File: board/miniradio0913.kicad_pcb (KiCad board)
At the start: 2 copper layers, 33 x 27.9 mm, 28 parts, among them J1 AudioJack3, J2 Conn_01x03_Socket, J3 USB_B_Micro, Q2 Q_PMOS_GSD, SW1 SW_Push, SW2 SW_Push, SW3 SW_Push, U1 CH32V003JxMx, U2 KT0913, U3 AQM0802, Y2 Crystal_GND2

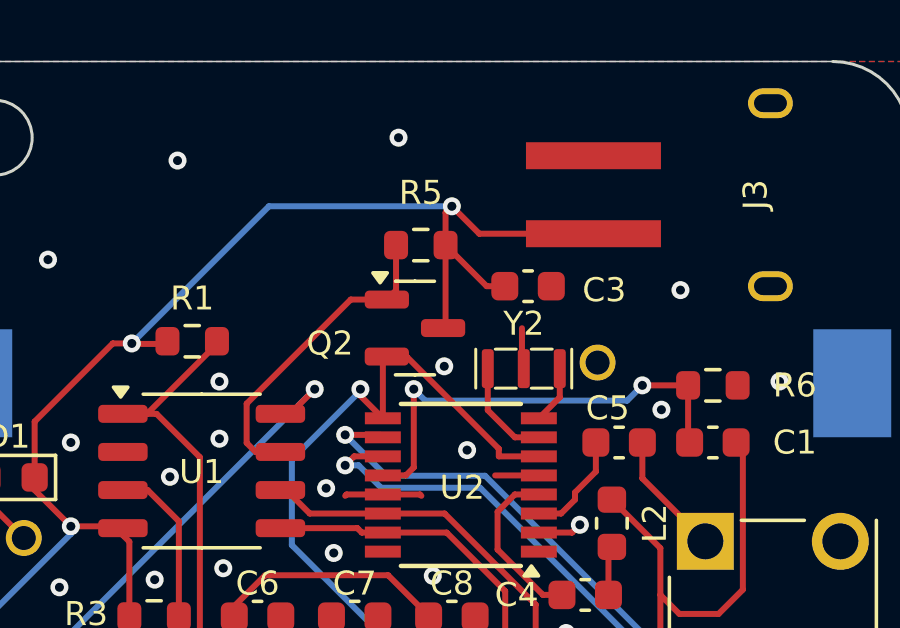
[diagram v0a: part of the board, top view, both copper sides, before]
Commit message: fix(board): crystal
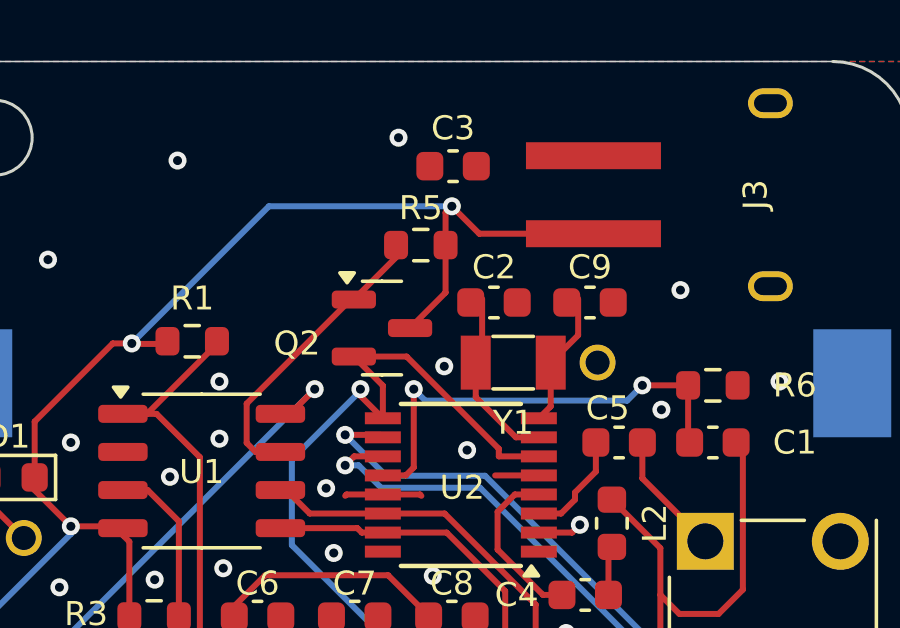
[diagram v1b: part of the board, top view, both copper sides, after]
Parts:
- removed Y2: Crystal_GND2, Library:SMD_Crystal_Murata
- added C2: 15p, Capacitor_SMD:C_0603_1608Metric, F.Cu at (57.3, 24.5)
- added C9: 15p, Capacitor_SMD:C_0603_1608Metric, F.Cu at (60.5, 24.5)
- added Y1: 32.768kHz, Crystal:Crystal_SMD_3215-2Pin_3.2x1.5mm, F.Cu at (57.9, 26.5)
- moved C3 4.72 mm to (55.9, 20.0)
- moved Q2 1.10 mm to (53.5, 25.4)
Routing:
- net Net-(U2-XO): track 1.94 -> 4.53 mm
- net Net-(U2-XI/RCLK): track 3.46 -> 6.03 mm
- net VDD: track 45.4 -> 43.3 mm
- net Net-(Q2-S): track 38.6 -> 40.1 mm
- net GND: track 28.8 -> 27.4 mm
- net Net-(Q2-G): track 10.6 -> 9.97 mm

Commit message: board: update
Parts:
- removed BT2: Battery, Library:CH25-2032LF
- removed D1: D_Small, Diode_SMD:D_0603_1608Metric
- removed J3: USB_B_Micro, Library:usb_microb_power_MRUSB-2B-D14NI-S306
- removed R1: R, Resistor_SMD:R_0603_1608Metric
- removed R5: 10k, Resistor_SMD:R_0603_1608Metric
- BT1: footprint Battery:BatteryHolder_Keystone_1060_1x2032 -> Library:BH-521_2xN
- J2, L1: moved to F.Cu
- moved L1 24.0 mm to (56.9, 19.1), turned to 0 degrees
- moved C3 20.6 mm to (41.9, 35.1)
- moved J2 8.85 mm to (36.2, 31.8), turned to 90 degrees
- moved BT1 3.47 mm to (53.3, 30.5)
- moved R2 3.33 mm to (41.9, 37.3), turned to 0 degrees
- moved J1 1.54 mm to (66.6, 37.5)
- moved C1 1.27 mm to (64.6, 27.9)
- moved R6 1.27 mm to (64.6, 26.0)
- moved Q2 0.76 mm to (53.5, 24.6), turned to 90 degrees
- moved C5 0.65 mm to (61.6, 28.6)
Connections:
- BT1 pad 1: Net-(BT1-+) -> VDD
- C6 pad 1: Net-(Q2-S) -> Net-(Q2-D)
- C8 pad 1: Net-(Q2-S) -> Net-(Q2-D)
- Q2 pad 2: Net-(Q2-S) -> VDD
- Q2 pad 3: VDD -> Net-(Q2-D)
- U2 pad 6: Net-(Q2-S) -> Net-(Q2-D)
- U2 pad 9: Net-(Q2-S) -> Net-(Q2-D)
- U3 pad 5: Net-(Q2-S) -> Net-(Q2-D)
- U3 pad 9: Net-(Q2-S) -> Net-(Q2-D)
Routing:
- net Net-(Q2-D): track 0.00 -> 40.4 mm, vias 0 -> 1
- net Net-(Q2-S): track 40.1 -> 0.00 mm, vias 1 -> 0
- net Net-(U2-AMINN): track 21.2 -> 13.7 mm
- net Net-(BT1-+): track 6.91 -> 0.00 mm, vias 1 -> 0
- net Net-(U2-AMINP): track 28.6 -> 22.6 mm
- net GND: track 27.4 -> 22.2 mm, vias 28 -> 27
- net Net-(U1-PD6/PA1): track 21.7 -> 17.6 mm
- net VDD: track 43.3 -> 39.6 mm, vias 3 -> 0
- net Net-(Q2-G): track 9.97 -> 7.09 mm
- net Net-(R2-Pad1): track 6.39 -> 8.72 mm
- net Net-(C1-Pad1): track 24.1 -> 22.0 mm
- net Net-(C5-Pad1): track 4.16 -> 3.20 mm
- net Net-(U2-ROUT): track 3.59 -> 4.28 mm
- net Net-(U2-RFINP): track 15.2 -> 15.8 mm
- net Net-(J2-Pin_2): track 18.7 -> 18.4 mm, vias 1 -> 2
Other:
- board size 33 x 27.9 mm -> 38.1 x 27.9 mm
- board text added: "+"
- board text added: "-"
- board text added: "Mini Radio v1"
- board text added: "●"
- board text removed: "Radio receiver"

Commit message: feat(board): update layout
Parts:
- BT1: moved to F.Cu
- J1, J2, L1, SW1, SW2, SW3, U3: moved to B.Cu
- moved L1 18.9 mm to (39.1, 25.4), turned to -90 degrees
- moved SW3 15.6 mm to (42.2, 40.8), turned to 180 degrees
- moved C6 12.1 mm to (61.5, 34.5), turned to 180 degrees
- moved SW1 9.86 mm to (54.9, 40.8), turned to 180 degrees
- moved C7 5.78 mm to (58.4, 34.5), turned to 180 degrees
- moved L2 5.37 mm to (66.3, 33.7)
- moved R2 5.29 mm to (47.0, 35.8), turned to 180 degrees
- moved C4 4.24 mm to (64.5, 33.7), turned to 90 degrees
- moved J1 3.59 mm to (66.3, 41.0), turned to 180 degrees
- moved SW2 3.00 mm to (48.6, 40.8), turned to 180 degrees
- moved C5 2.88 mm to (63.8, 30.5)
- moved R3 2.65 mm to (43.4, 35.8)
- moved C3 1.97 mm to (43.4, 33.8)
- moved U3 1.56 mm to (56.1, 36.4), turned to 180 degrees
- moved J2 1.02 mm to (36.1, 30.7), turned to -90 degrees
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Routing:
- net GND: track 22.2 -> 8.20 mm, vias 27 -> 25
- net Net-(C5-Pad1): track 3.20 -> 11.2 mm, vias 0 -> 1
- net Net-(Q2-D): track 40.4 -> 32.9 mm, vias 1 -> 0
- net Net-(R2-Pad1): track 8.72 -> 14.4 mm, vias 0 -> 1
- net Net-(C1-Pad1): track 22.0 -> 16.8 mm
- net Net-(J2-Pin_2): track 18.4 -> 23.1 mm, vias 2 -> 3
- net Net-(U2-LOUT): track 5.65 -> 10.2 mm
- net Net-(U1-PD6/PA1): track 17.6 -> 21.7 mm, vias 0 -> 1
- net Net-(U2-AMINN): track 13.7 -> 17.5 mm
- net Net-(U1-PC1): track 11.1 -> 9.00 mm
- net VDD: track 39.6 -> 41.4 mm
- net Net-(U1-PC2): track 12.7 -> 11.1 mm
- net Net-(U2-AMINP): track 22.6 -> 21.1 mm
- net Net-(U1-PA2): track 26.9 -> 27.9 mm, vias 0 -> 1
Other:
- board size 38.1 x 27.9 mm -> 38.1 x 28.9 mm
- board text added: "Mini Radio v2"
- board text removed: "Mini Radio v1"

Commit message: board: update
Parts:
- added C10: 0.1u, Capacitor_SMD:C_0603_1608Metric, F.Cu at (42.9, 31.5)
- moved C3 7.92 mm to (45.1, 26.0)
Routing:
- net VDD: track 41.4 -> 40.7 mm
- net GND: vias 25 -> 40
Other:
- board size 38.1 x 28.9 mm -> 38.1 x 30.2 mm

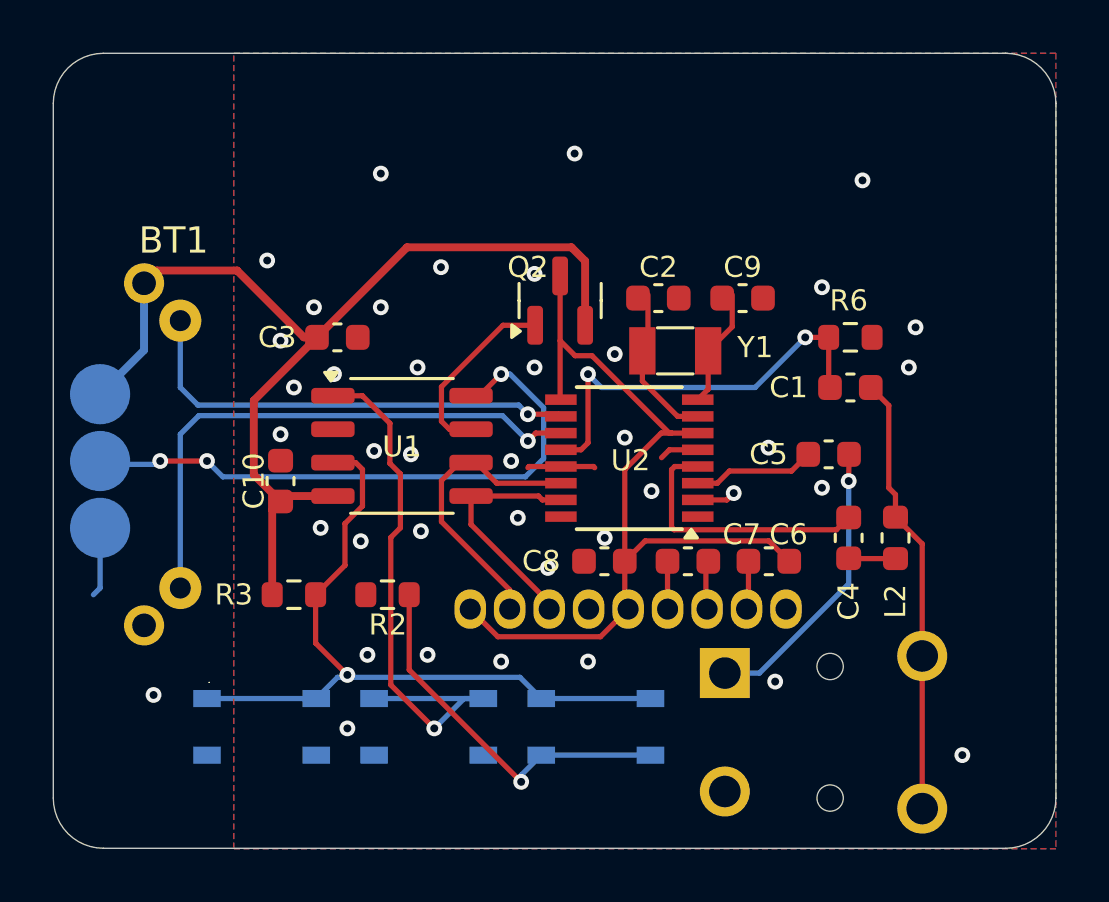
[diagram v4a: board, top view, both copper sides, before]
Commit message: board: renumber parts
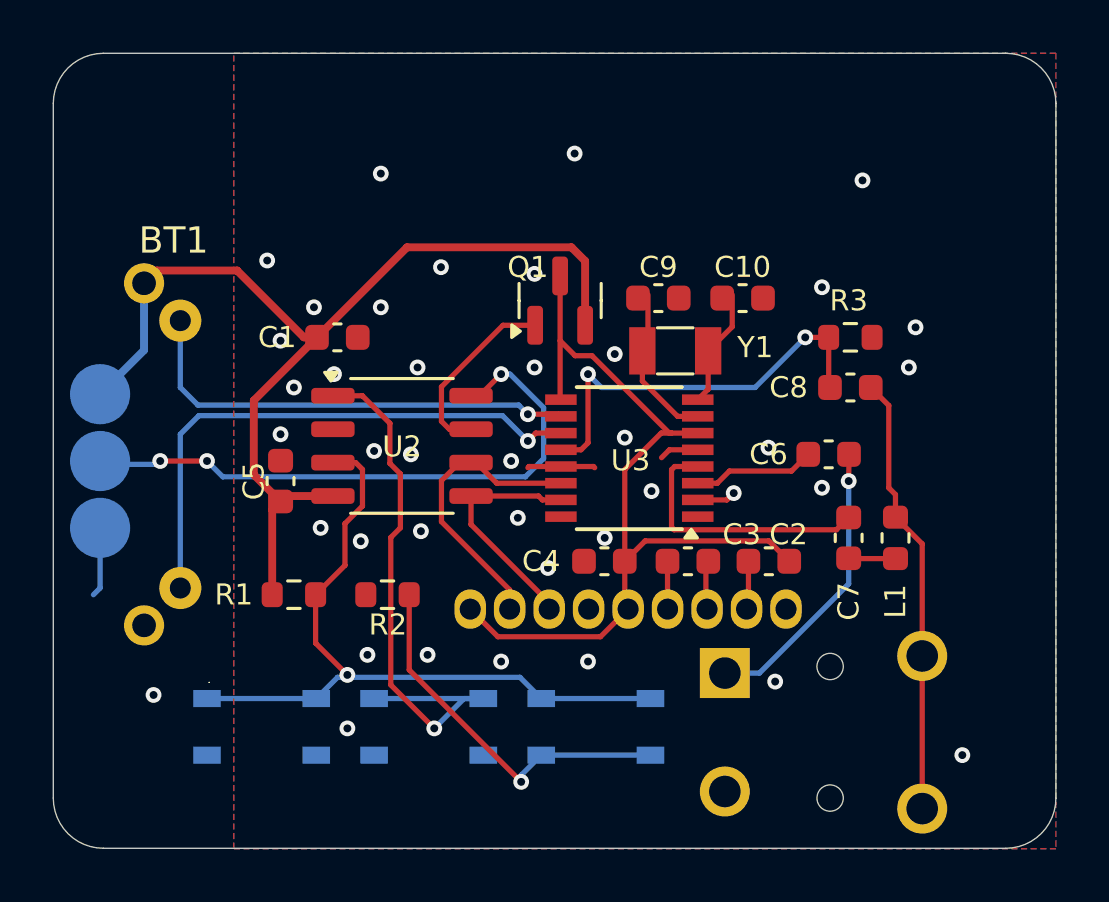
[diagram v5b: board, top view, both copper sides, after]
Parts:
- renumbered C3 to C1, C9 to C10, C6 to C2, C7 to C3, C8 to C4, C10 to C5, C5 to C6, C4 to C7, C1 to C8, C2 to C9, J2 to J1, J1 to J2, L2 to L1, L1 to L2, Q2 to Q1, R3 to R1, R6 to R3, SW2 to SW1, SW1 to SW2, U3 to U1, U1 to U2, U2 to U3

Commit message: board: fix wiring
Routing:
- net GND: track 8.20 -> 15.3 mm
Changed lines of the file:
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@@
 		(start 58.78 30.3075)
 		(end 57.7035 30.3075)
-		(width 0.2)
+		(width 0.3)
 		(layer "F.Cu")
 		(net 3)
@@
 		(start 53.58 30.9425)
 		(end 52.3695 30.9425)
-		(width 0.2)
+		(width 0.3)
 		(layer "F.Cu")
 		(net 3)
@@
 		(start 60.1472 31.9532)
 		(end 59.8879 32.2125)
-		(width 0.2)
+		(width 0.3)
 		(layer "F.Cu")
 		(net 3)
@@
 		(start 53.58 30.9425)
 		(end 54.8185 30.9425)
-		(width 0.2)
+		(width 0.3)
 		(layer "F.Cu")
 		(net 3)
@@
 		(start 52.324 30.988)
 		(end 52.3695 30.9425)
-		(width 0.2)
+		(width 0.3)
 		(layer "F.Cu")
 		(net 3)
@@
 		(start 54.864 30.988)
 		(end 54.8185 30.9425)
-		(width 0.2)
+		(width 0.3)
 		(layer "F.Cu")
 		(net 3)
@@
 		(start 59.8879 32.2125)
 		(end 58.78 32.2125)
-		(width 0.2)
+		(width 0.3)
 		(layer "F.Cu")
 		(net 3)
@@
 		(start 57.7035 30.3075)
 		(end 57.404 30.607)
-		(width 0.2)
+		(width 0.3)
+		(layer "F.Cu")
+		(net 3)
+	)
+	(segment
+		(start 37.74 36.98)
+		(end 41.656 36.98)
+		(width 0.3)
 		(layer "F.Cu")
 		(net 3)
@@
 	)
 	(via
+		(at 41.656 36.98)
+		(size 0.6)
+		(drill 0.3)
+		(layers "F.Cu" "B.Cu")
+		(net 3)
+	)
+	(via
 		(at 60.1472 31.9532)
 		(size 0.6)
@@
 	)
 	(via
-		(at 38.1 39.624)
-		(size 0.6)
-		(drill 0.3)
-		(layers "F.Cu" "B.Cu")
-		(free yes)
-		(net 3)
-	)
-	(via
 		(at 57.023 31.877)
 		(size 0.6)
@@
 	)
 	(segment
-		(start 36.068 35.56)
-		(end 35.814 35.814)
-		(width 0.2)
+		(start 41.656 36.98)
+		(end 41.806 36.98)
+		(width 0.3)
 		(layer "B.Cu")
 		(net 3)
 	)
 	(segment
+		(start 36.068 35.308)
+		(end 37.74 36.98)
+		(width 0.3)
+		(layer "B.Cu")
+		(net 3)
+	)
+	(segment
 		(start 36.068 33.274)
-		(end 36.068 35.56)
-		(width 0.2)
+		(end 36.068 35.308)
+		(width 0.3)
 		(layer "B.Cu")
 		(net 3)
+	)
+	(segment
+		(start 40.132 41.91)
+		(end 41.402 41.91)
+		(width 0.3)
+		(layer "B.Cu")
+		(net 3)

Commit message: update board
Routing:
- net GND: vias 40 -> 43
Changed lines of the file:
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@@
 		(start 43.815 26.035)
 		(end 44.565592 26.035)
-		(width 0.3)
+		(width 0.4)
 		(layer "F.Cu")
 		(net 2)
@@
 		(start 41.275 23.495)
 		(end 43.815 26.035)
-		(width 0.3)
-		(layer "F.Cu")
-		(net 2)
-	)
-	(segment
-		(start 47.732 22.613)
-		(end 41.91 28.435)
-		(width 0.3)
-		(layer "F.Cu")
-		(net 2)
-	)
-	(segment
-		(start 41.91 28.435)
-		(end 41.91 31.255)
-		(width 0.3)
+		(width 0.4)
+		(layer "F.Cu")
+		(net 2)
+	)
+	(segment
+		(start 53.848 22.479)
+		(end 47.866 22.479)
+		(width 0.4)
+		(layer "F.Cu")
+		(net 2)
+	)
+	(segment
+		(start 42.037 31.382)
+		(end 42.926 32.271)
+		(width 0.4)
+		(layer "F.Cu")
+		(net 2)
+	)
+	(segment
+		(start 42.037 28.308)
+		(end 42.037 31.382)
+		(width 0.4)
+		(layer "F.Cu")
+		(net 2)
+	)
+	(segment
+		(start 54.5 23.131)
+		(end 53.848 22.479)
+		(width 0.4)
+		(layer "F.Cu")
+		(net 2)
+	)
+	(segment
+		(start 42.609 32.588)
+		(end 42.926 32.271)
+		(width 0.4)
+		(layer "F.Cu")
+		(net 2)
+	)
+	(segment
+		(start 37.74 23.98)
+		(end 38.225 23.495)
+		(width 0.4)
+		(layer "F.Cu")
+		(net 2)
+	)
+	(segment
+		(start 42.609 35.814)
+		(end 42.609 32.588)
+		(width 0.4)
+		(layer "F.Cu")
+		(net 2)
+	)
+	(segment
+		(start 42.926 32.271)
+		(end 43.132 32.065)
+		(width 0.4)
+		(layer "F.Cu")
+		(net 2)
+	)
+	(segment
+		(start 43.132 32.065)
+		(end 44.915 32.065)
+		(width 0.4)
+		(layer "F.Cu")
+		(net 2)
+	)
+	(segment
+		(start 38.225 23.495)
+		(end 41.275 23.495)
+		(width 0.4)
+		(layer "F.Cu")
+		(net 2)
+	)
+	(segment
+		(start 47.866 22.479)
+		(end 42.037 28.308)
+		(width 0.4)
 		(layer "F.Cu")
 		(net 2)
@@
 		(start 54.5 25.5755)
 		(end 54.5 23.131)
-		(width 0.3)
-		(layer "F.Cu")
-		(net 2)
-	)
-	(segment
-		(start 41.91 31.255)
-		(end 42.926 32.271)
-		(width 0.3)
-		(layer "F.Cu")
-		(net 2)
-	)
-	(segment
-		(start 42.609 32.588)
-		(end 42.926 32.271)
-		(width 0.3)
-		(layer "F.Cu")
-		(net 2)
-	)
-	(segment
-		(start 54.5 23.131)
-		(end 53.982 22.613)
-		(width 0.3)
-		(layer "F.Cu")
-		(net 2)
-	)
-	(segment
-		(start 37.74 23.98)
-		(end 38.225 23.495)
-		(width 0.3)
-		(layer "F.Cu")
-		(net 2)
-	)
-	(segment
-		(start 42.609 35.814)
-		(end 42.609 32.588)
-		(width 0.3)
-		(layer "F.Cu")
-		(net 2)
-	)
-	(segment
-		(start 42.926 32.271)
-		(end 43.132 32.065)
-		(width 0.3)
-		(layer "F.Cu")
-		(net 2)
-	)
-	(segment
-		(start 43.132 32.065)
-		(end 44.915 32.065)
-		(width 0.3)
-		(layer "F.Cu")
-		(net 2)
-	)
-	(segment
-		(start 38.225 23.495)
-		(end 41.275 23.495)
-		(width 0.3)
-		(layer "F.Cu")
-		(net 2)
-	)
-	(segment
-		(start 53.982 22.613)
-		(end 47.732 22.613)
-		(width 0.3)
+		(width 0.4)
 		(layer "F.Cu")
 		(net 2)
@@
 		(start 36.068 28.194)
 		(end 37.74 26.522)
-		(width 0.3)
+		(width 0.4)
 		(layer "B.Cu")
 		(net 2)
@@
 		(start 37.74 26.522)
 		(end 37.74 23.98)
-		(width 0.3)
+		(width 0.4)
 		(layer "B.Cu")
 		(net 2)
@@
 		(start 58.78 30.3075)
 		(end 57.7035 30.3075)
-		(width 0.3)
+		(width 0.4)
 		(layer "F.Cu")
 		(net 3)
@@
 		(start 53.58 30.9425)
 		(end 52.3695 30.9425)
-		(width 0.3)
+		(width 0.4)
 		(layer "F.Cu")
 		(net 3)
@@
 		(start 60.1472 31.9532)
 		(end 59.8879 32.2125)
-		(width 0.3)
+		(width 0.4)
 		(layer "F.Cu")
 		(net 3)
@@
 		(start 53.58 30.9425)
 		(end 54.8185 30.9425)
-		(width 0.3)
+		(width 0.4)
 		(layer "F.Cu")
 		(net 3)
@@
 		(start 52.324 30.988)
 		(end 52.3695 30.9425)
-		(width 0.3)
+		(width 0.4)
 		(layer "F.Cu")
 		(net 3)
@@
 		(start 54.864 30.988)
 		(end 54.8185 30.9425)
-		(width 0.3)
+		(width 0.4)
 		(layer "F.Cu")
 		(net 3)
@@
 		(start 59.8879 32.2125)
 		(end 58.78 32.2125)
-		(width 0.3)
+		(width 0.4)
 		(layer "F.Cu")
 		(net 3)
@@
 		(start 57.7035 30.3075)
 		(end 57.404 30.607)
-		(width 0.3)
+		(width 0.4)
 		(layer "F.Cu")
 		(net 3)
@@
 		(start 37.74 36.98)
 		(end 41.656 36.98)
-		(width 0.3)
+		(width 0.4)
 		(layer "F.Cu")
 		(net 3)
@@
 	)
 	(via
+		(at 41.275 30.099)
+		(size 0.6)
+		(drill 0.3)
+		(layers "F.Cu" "B.Cu")
+		(free yes)
+		(net 3)
+	)
+	(via
 		(at 53.086 34.798)
 		(size 0.6)
@@
 	)
 	(via
+		(at 41.529 32.131)
+		(size 0.6)
+		(drill 0.3)
+		(layers "F.Cu" "B.Cu")
+		(free yes)
+		(net 3)
+	)
+	(via
 		(at 65.040513 20.069211)
 		(size 0.6)
@@
 	)
 	(via
-		(at 47.879 30.48)
+		(at 48.26 30.353)
 		(size 0.6)
 		(drill 0.3)
@@
 	(via
 		(at 42.926 26.162)
+		(size 0.6)
+		(drill 0.3)
+		(layers "F.Cu" "B.Cu")
+		(free yes)
+		(net 3)
+	)
+	(via
+		(at 41.402 27.686)
 		(size 0.6)
 		(drill 0.3)
@@
 		(start 41.656 36.98)
 		(end 41.806 36.98)
-		(width 0.3)
+		(width 0.4)
 		(layer "B.Cu")
 		(net 3)
@@
 		(start 36.068 35.308)
 		(end 37.74 36.98)
-		(width 0.3)
+		(width 0.4)
 		(layer "B.Cu")
 		(net 3)
@@
 		(start 36.068 33.274)
 		(end 36.068 35.308)
-		(width 0.3)
+		(width 0.4)
 		(layer "B.Cu")
 		(net 3)
@@
 		(start 40.132 41.91)
 		(end 41.402 41.91)
-		(width 0.3)
+		(width 0.4)
 		(layer "B.Cu")
 		(net 3)
@@
 	)
 	(segment
-		(start 47.115 33.639)
-		(end 47.48 33.274)
+		(start 46.035 28.255)
+		(end 44.915 28.255)
+		(width 0.2)
+		(layer "F.Cu")
+		(net 20)
+	)
+	(segment
+		(start 48.768 40.894)
+		(end 47.115 39.241)
 		(width 0.2)
 		(layer "F.Cu")
@@
 	)
 	(segment
-		(start 46.035 28.255)
-		(end 44.915 28.255)
+		(start 47.625 29.845)
+		(end 46.035 28.255)
 		(width 0.2)
 		(layer "F.Cu")
@@
 	)
 	(segment
-		(start 47.48 31.223999)
-		(end 47.082 30.825999)
+		(start 47.625 33.129)
+		(end 47.625 29.845)
 		(width 0.2)
 		(layer "F.Cu")
@@
 	)
 	(segment
-		(start 48.768 40.894)
-		(end 47.115 39.241)
-		(width 0.2)
-		(layer "F.Cu")
-		(net 20)
-	)
-	(segment
-		(start 47.082 29.302)
-		(end 46.035 28.255)
-		(width 0.2)
-		(layer "F.Cu")
-		(net 20)
-	)
-	(segment
-		(start 47.48 33.274)
-		(end 47.48 31.223999)
-		(width 0.2)
-		(layer "F.Cu")
-		(net 20)
-	)
-	(segment
-		(start 47.082 30.825999)
-		(end 47.082 29.302)
-		(width 0.2)
-		(layer "F.Cu")
+		(start 47.115 33.639)
+		(end 47.625 33.129)
+		(width 0.2)
+		(layer "F.Cu")
